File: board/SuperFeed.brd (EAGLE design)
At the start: 97.8 x 59.7 mm, 16 parts

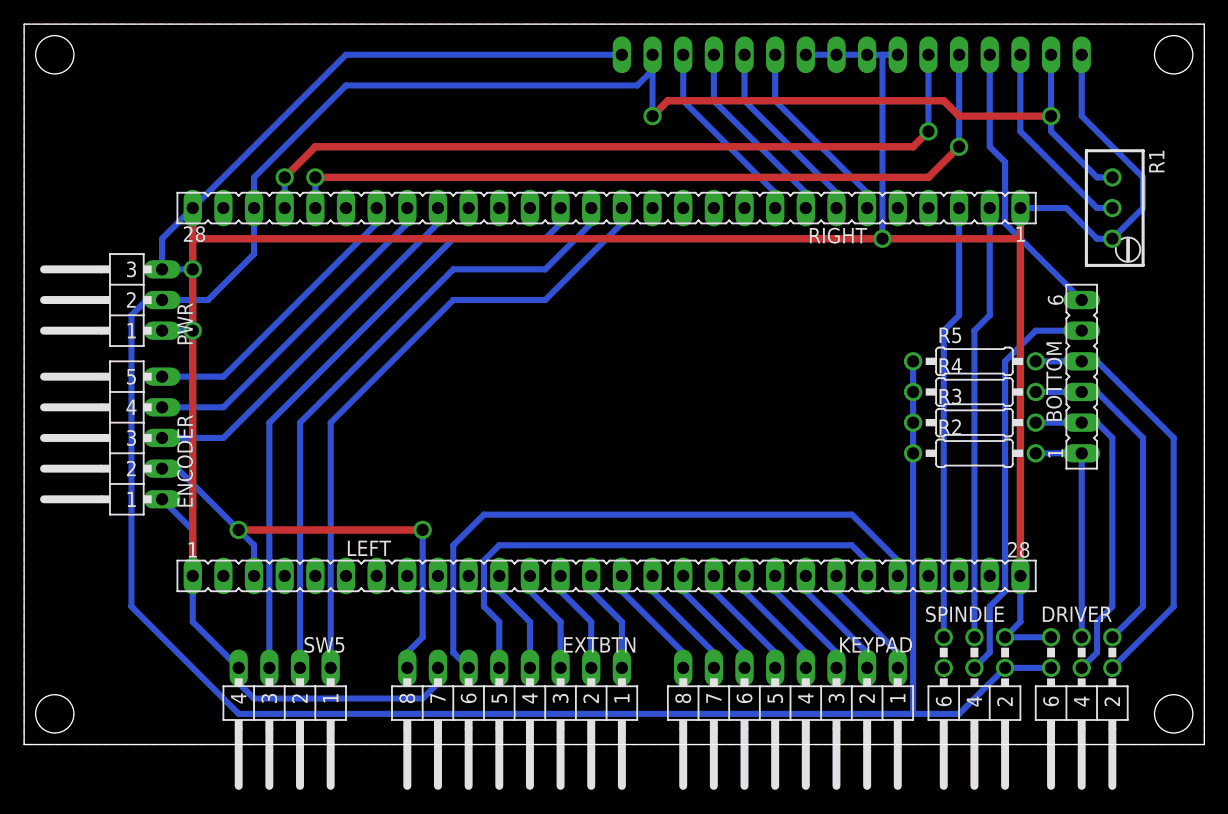
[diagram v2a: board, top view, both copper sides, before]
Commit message: Re-routing board to use GND plane on bottom side
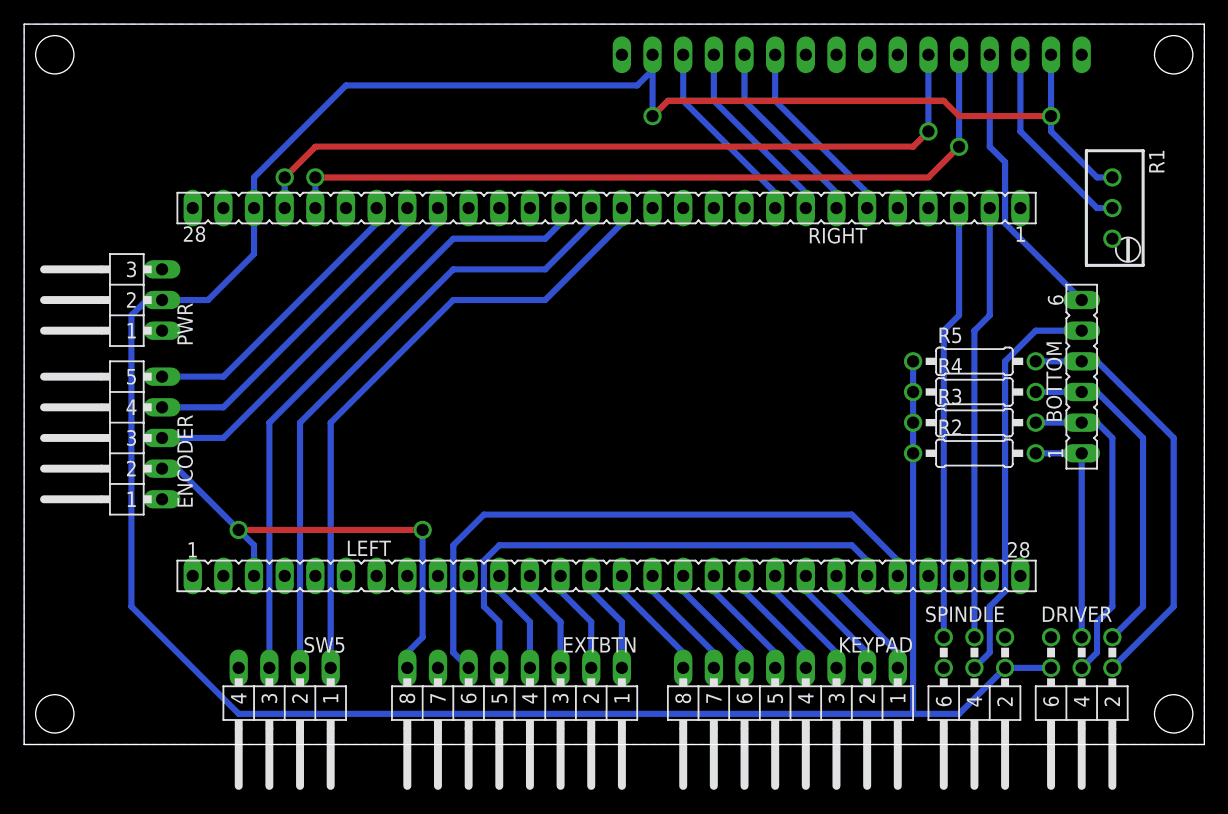
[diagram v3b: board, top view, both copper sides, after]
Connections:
- net GND: no longer PWR.1
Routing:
- net GND: track 278.9 -> 0.00 mm, vias 3 -> 0
- added copper zone on layer 16, net GND
- removed copper zone on layer 1, net GND
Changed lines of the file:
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@@
 <?xml version="1.0" encoding="utf-8"?>
 <!DOCTYPE eagle SYSTEM "eagle.dtd">
-<eagle version="6.2">
+<eagle version="6.6.0">
 <drawing>
 <settings>
@@
 <layer number="17" name="Pads" color="2" fill="1" visible="yes" active="yes"/>
 <layer number="18" name="Vias" color="2" fill="1" visible="yes" active="yes"/>
-<layer number="19" name="Unrouted" color="6" fill="1" visible="no" active="yes"/>
+<layer number="19" name="Unrouted" color="6" fill="1" visible="yes" active="yes"/>
 <layer number="20" name="Dimension" color="15" fill="1" visible="yes" active="yes"/>
 <layer number="21" name="tPlace" color="7" fill="1" visible="no" active="yes"/>
-<layer number="22" name="bPlace" color="7" fill="1" visible="no" active="yes"/>
-<layer number="23" name="tOrigins" color="15" fill="1" visible="no" active="yes"/>
-<layer number="24" name="bOrigins" color="15" fill="1" visible="no" active="yes"/>
+<layer number="22" name="bPlace" color="7" fill="1" visible="yes" active="yes"/>
+<layer number="23" name="tOrigins" color="15" fill="1" visible="yes" active="yes"/>
+<layer number="24" name="bOrigins" color="15" fill="1" visible="yes" active="yes"/>
 <layer number="25" name="tNames" color="7" fill="1" visible="no" active="yes"/>
 <layer number="26" name="bNames" color="7" fill="1" visible="no" active="yes"/>
@@
 <layer number="43" name="vRestrict" color="2" fill="10" visible="no" active="yes"/>
 <layer number="44" name="Drills" color="7" fill="1" visible="no" active="yes"/>
-<layer number="45" name="Holes" color="7" fill="1" visible="yes" active="yes"/>
+<layer number="45" name="Holes" color="7" fill="1" visible="no" active="yes"/>
 <layer number="46" name="Milling" color="3" fill="1" visible="no" active="yes"/>
 <layer number="47" name="Measures" color="7" fill="1" visible="no" active="yes"/>
@@
 </class>
 </classes>
-<designrules>
+<designrules name="default">
 <description language="de">&lt;b&gt;EAGLE Design Rules&lt;/b&gt;
 &lt;p&gt;
@@
 <contactref element="SPINDLE" pad="1"/>
 <contactref element="DRIVER" pad="5"/>
-<wire x1="85.09" y1="8.89" x2="81.28" y2="8.89" width="0.508" layer="16"/>
-<wire x1="82.55" y1="13.97" x2="82.55" y2="12.7" width="0.508" layer="16"/>
-<wire x1="64.77" y1="57.15" x2="67.31" y2="57.15" width="0.508" layer="16"/>
-<wire x1="67.31" y1="57.15" x2="69.85" y2="57.15" width="0.508" layer="16"/>
-<wire x1="69.85" y1="57.15" x2="71.12" y2="57.15" width="0.508" layer="16"/>
-<wire x1="13.97" y1="10.16" x2="13.97" y2="13.97" width="0.508" layer="16"/>
-<wire x1="13.97" y1="13.97" x2="13.97" y2="17.78" width="0.508" layer="16"/>
-<wire x1="13.97" y1="17.78" x2="11.43" y2="20.32" width="0.508" layer="16"/>
-<wire x1="49.53" y1="57.15" x2="26.67" y2="57.15" width="0.508" layer="16"/>
-<wire x1="82.55" y1="13.97" x2="82.55" y2="10.16" width="0.508" layer="16"/>
-<wire x1="82.55" y1="10.16" x2="81.28" y2="8.89" width="0.508" layer="16"/>
-<wire x1="82.55" y1="13.97" x2="82.55" y2="41.91" width="0.6096" layer="1"/>
-<wire x1="13.97" y1="13.97" x2="13.97" y2="34.29" width="0.6096" layer="1"/>
-<wire x1="13.97" y1="39.37" x2="13.97" y2="41.91" width="0.6096" layer="1"/>
-<wire x1="13.97" y1="41.91" x2="71.12" y2="41.91" width="0.6096" layer="1"/>
 <contactref element="R1" pad="3"/>
-<wire x1="82.55" y1="44.45" x2="86.36" y2="44.45" width="0.508" layer="16"/>
-<wire x1="86.36" y1="44.45" x2="88.9" y2="41.91" width="0.508" layer="16"/>
-<wire x1="88.9" y1="41.91" x2="90.17" y2="41.91" width="0.508" layer="16"/>
-<wire x1="87.63" y1="57.15" x2="87.63" y2="52.07" width="0.508" layer="16"/>
-<wire x1="87.63" y1="52.07" x2="92.71" y2="46.99" width="0.508" layer="16"/>
-<wire x1="92.71" y1="46.99" x2="92.71" y2="44.45" width="0.508" layer="16"/>
-<wire x1="92.71" y1="44.45" x2="90.17" y2="41.91" width="0.508" layer="16"/>
-<wire x1="17.78" y1="6.35" x2="13.97" y2="10.16" width="0.508" layer="16"/>
-<wire x1="72.39" y1="57.15" x2="71.12" y2="57.15" width="0.508" layer="16"/>
-<wire x1="71.12" y1="57.15" x2="71.12" y2="41.91" width="0.508" layer="16"/>
-<via x="71.12" y="41.91" extent="1-16" drill="1.016"/>
-<wire x1="82.55" y1="44.45" x2="82.55" y2="41.91" width="0.6096" layer="1"/>
-<wire x1="82.55" y1="41.91" x2="71.12" y2="41.91" width="0.6096" layer="1"/>
-<wire x1="13.97" y1="44.45" x2="13.97" y2="41.91" width="0.6096" layer="1"/>
-<contactref element="PWR" pad="1"/>
-<wire x1="11.43" y1="34.29" x2="13.97" y2="34.29" width="0.508" layer="16"/>
-<via x="13.97" y="34.29" extent="1-16" drill="1.016"/>
-<wire x1="11.43" y1="39.37" x2="13.97" y2="39.37" width="0.508" layer="16"/>
-<via x="13.97" y="39.37" extent="1-16" drill="1.016"/>
-<wire x1="13.97" y1="39.37" x2="13.97" y2="34.29" width="0.6096" layer="1"/>
-<wire x1="13.97" y1="44.45" x2="11.43" y2="41.91" width="0.508" layer="16"/>
-<wire x1="11.43" y1="39.37" x2="11.43" y2="41.91" width="0.508" layer="16"/>
-<wire x1="13.97" y1="44.45" x2="26.67" y2="57.15" width="0.508" layer="16"/>
-<polygon width="0.4064" layer="1" isolate="0.4064" rank="6">
+<contactref element="EXTBTN" pad="7"/>
+<polygon width="0.508" layer="16">
+<vertex x="0" y="59.69"/>
 <vertex x="97.79" y="59.69"/>
 <vertex x="97.79" y="0"/>
 <vertex x="0" y="0"/>
-<vertex x="0" y="59.69"/>
 </polygon>
-<contactref element="EXTBTN" pad="7"/>
-<wire x1="34.29" y1="6.35" x2="34.29" y2="5.08" width="0.508" layer="16"/>
-<wire x1="34.29" y1="5.08" x2="33.02" y2="3.81" width="0.508" layer="16"/>
-<wire x1="33.02" y1="3.81" x2="19.05" y2="3.81" width="0.508" layer="16"/>
-<wire x1="19.05" y1="3.81" x2="17.78" y2="5.08" width="0.508" layer="16"/>
-<wire x1="17.78" y1="5.08" x2="17.78" y2="6.35" width="0.508" layer="16"/>
+<wire x1="49.53" y1="57.15" x2="64.77" y2="57.15" width="0" layer="19" extent="1-1"/>
 </signal>
 <signal name="+5V">
@@
 <wire x1="85.09" y1="50.8" x2="85.09" y2="52.07" width="0.508" layer="16"/>
 <via x="85.09" y="52.07" extent="1-16" drill="1.016"/>
-<wire x1="85.09" y1="52.07" x2="77.47" y2="52.07" width="0.6096" layer="1"/>
-<wire x1="77.47" y1="52.07" x2="76.2" y2="53.34" width="0.6096" layer="1"/>
-<wire x1="76.2" y1="53.34" x2="53.34" y2="53.34" width="0.6096" layer="1"/>
-<wire x1="53.34" y1="53.34" x2="52.07" y2="52.07" width="0.6096" layer="1"/>
+<wire x1="85.09" y1="52.07" x2="77.47" y2="52.07" width="0.508" layer="1"/>
+<wire x1="77.47" y1="52.07" x2="76.2" y2="53.34" width="0.508" layer="1"/>
+<wire x1="76.2" y1="53.34" x2="53.34" y2="53.34" width="0.508" layer="1"/>
+<wire x1="53.34" y1="53.34" x2="52.07" y2="52.07" width="0.508" layer="1"/>
 <wire x1="11.43" y1="36.83" x2="15.24" y2="36.83" width="0.508" layer="16"/>
 <wire x1="15.24" y1="36.83" x2="19.05" y2="40.64" width="0.508" layer="16"/>
@@
 <wire x1="33.02" y1="8.89" x2="33.02" y2="17.78" width="0.508" layer="16"/>
 <via x="33.02" y="17.78" extent="1-16" drill="1.016"/>
-<wire x1="33.02" y1="17.78" x2="17.78" y2="17.78" width="0.6096" layer="1"/>
+<wire x1="33.02" y1="17.78" x2="17.78" y2="17.78" width="0.508" layer="1"/>
 <via x="17.78" y="17.78" extent="1-16" drill="1.016"/>
 <wire x1="17.78" y1="17.78" x2="19.05" y2="16.51" width="0.508" layer="16"/>
@@
 <wire x1="74.93" y1="57.15" x2="74.93" y2="50.8" width="0.508" layer="16"/>
 <via x="74.93" y="50.8" extent="1-16" drill="1.016"/>
-<wire x1="74.93" y1="50.8" x2="73.66" y2="49.53" width="0.6096" layer="1"/>
-<wire x1="73.66" y1="49.53" x2="24.13" y2="49.53" width="0.6096" layer="1"/>
-<wire x1="24.13" y1="49.53" x2="21.59" y2="46.99" width="0.6096" layer="1"/>
+<wire x1="74.93" y1="50.8" x2="73.66" y2="49.53" width="0.508" layer="1"/>
+<wire x1="73.66" y1="49.53" x2="24.13" y2="49.53" width="0.508" layer="1"/>
+<wire x1="24.13" y1="49.53" x2="21.59" y2="46.99" width="0.508" layer="1"/>
 <via x="21.59" y="46.99" extent="1-16" drill="1.016"/>
 <wire x1="21.59" y1="46.99" x2="21.59" y2="44.45" width="0.508" layer="16"/>
@@
 <wire x1="77.47" y1="57.15" x2="77.47" y2="49.53" width="0.508" layer="16"/>
 <via x="77.47" y="49.53" extent="1-16" drill="1.016"/>
-<wire x1="77.47" y1="49.53" x2="74.93" y2="46.99" width="0.6096" layer="1"/>
-<wire x1="74.93" y1="46.99" x2="24.13" y2="46.99" width="0.6096" layer="1"/>
+<wire x1="77.47" y1="49.53" x2="74.93" y2="46.99" width="0.508" layer="1"/>
+<wire x1="74.93" y1="46.99" x2="24.13" y2="46.99" width="0.508" layer="1"/>
 <via x="24.13" y="46.99" extent="1-16" drill="1.016"/>
 <wire x1="24.13" y1="46.99" x2="24.13" y2="44.45" width="0.508" layer="16"/>

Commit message: Custom design rules, moving pot a little bit
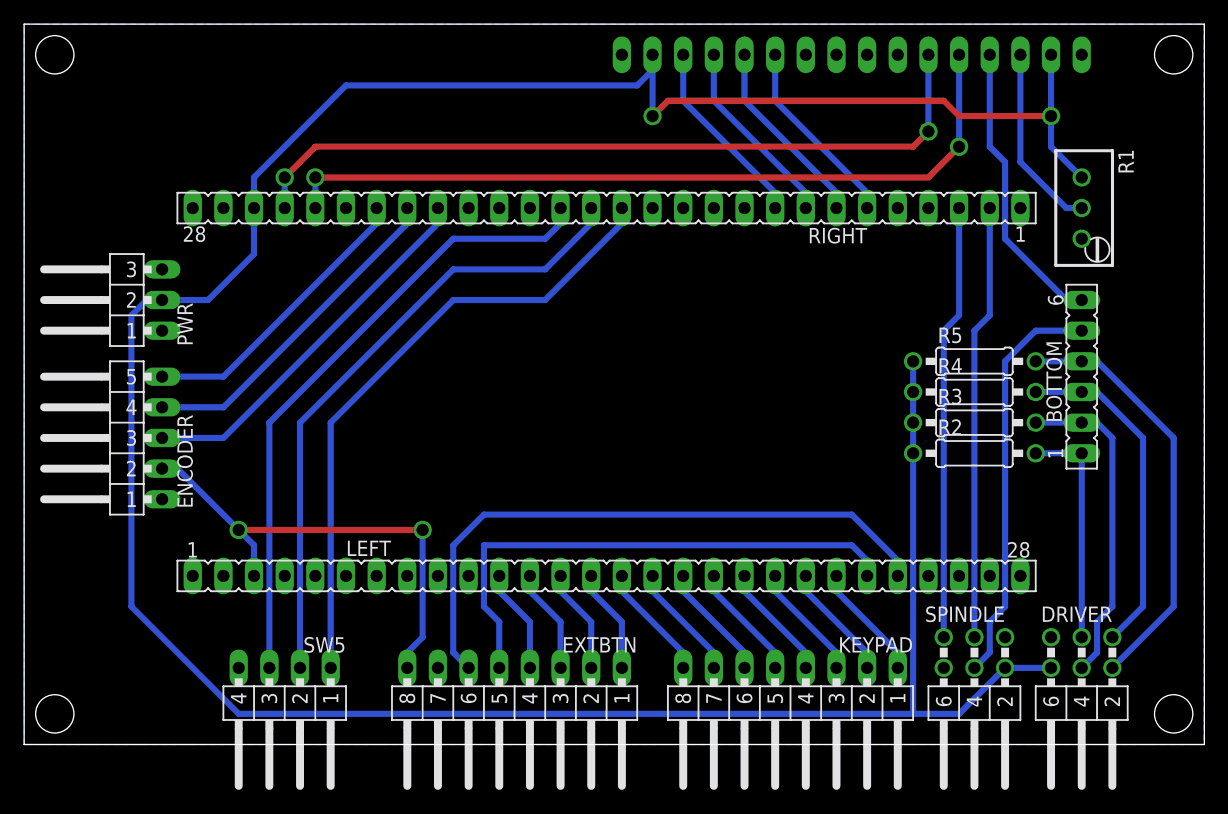
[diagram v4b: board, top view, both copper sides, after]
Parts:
- moved R1 2.54 mm to (87.6, 44.5)
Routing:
- net +5V: track 243.5 -> 241.8 mm
- net V0: track 16.6 -> 15.5 mm
- net PB15: track 23.5 -> 24.2 mm
- net PC4: track 43.5 -> 44.2 mm
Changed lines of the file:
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@@
 </class>
 </classes>
-<designrules name="default">
+<designrules name="SuperFeed">
 <description language="de">&lt;b&gt;EAGLE Design Rules&lt;/b&gt;
 &lt;p&gt;
@@
 <param name="mtCopper" value="0.035mm 0.035mm 0.035mm 0.035mm 0.035mm 0.035mm 0.035mm 0.035mm 0.035mm 0.035mm 0.035mm 0.035mm 0.035mm 0.035mm 0.035mm 0.035mm"/>
 <param name="mtIsolate" value="1.5mm 0.15mm 0.2mm 0.15mm 0.2mm 0.15mm 0.2mm 0.15mm 0.2mm 0.15mm 0.2mm 0.15mm 0.2mm 0.15mm 0.2mm"/>
-<param name="mdWireWire" value="8mil"/>
-<param name="mdWirePad" value="8mil"/>
-<param name="mdWireVia" value="8mil"/>
-<param name="mdPadPad" value="8mil"/>
-<param name="mdPadVia" value="8mil"/>
-<param name="mdViaVia" value="8mil"/>
-<param name="mdSmdPad" value="8mil"/>
-<param name="mdSmdVia" value="8mil"/>
-<param name="mdSmdSmd" value="8mil"/>
+<param name="mdWireWire" value="10mil"/>
+<param name="mdWirePad" value="10mil"/>
+<param name="mdWireVia" value="10mil"/>
+<param name="mdPadPad" value="10mil"/>
+<param name="mdPadVia" value="10mil"/>
+<param name="mdViaVia" value="10mil"/>
+<param name="mdSmdPad" value="10mil"/>
+<param name="mdSmdVia" value="10mil"/>
+<param name="mdSmdSmd" value="10mil"/>
 <param name="mdViaViaSameLayer" value="8mil"/>
 <param name="mnLayersViaInSmd" value="2"/>
 <param name="mdCopperDimension" value="40mil"/>
-<param name="mdDrill" value="8mil"/>
+<param name="mdDrill" value="10mil"/>
 <param name="mdSmdStop" value="0mil"/>
-<param name="msWidth" value="10mil"/>
+<param name="msWidth" value="16mil"/>
 <param name="msDrill" value="24mil"/>
 <param name="msMicroVia" value="9.99mm"/>
@@
 <param name="srMaxRoundness" value="0mil"/>
 <param name="slThermalIsolate" value="10mil"/>
-<param name="slThermalsForVias" value="0"/>
+<param name="slThermalsForVias" value="1"/>
 <param name="dpMaxLengthDifference" value="10mm"/>
 <param name="dpGapFactor" value="2.5"/>
@@
 <element name="PWR" library="SuperFeed" package="MA03-1W" value="" x="11.43" y="36.83" rot="R90"/>
 <element name="SPINDLE" library="SuperFeed" package="MA03-2W" value="" x="78.74" y="7.62" rot="R180"/>
-<element name="R1" library="SuperFeed" package="RTRIMT93YA" value="" x="90.17" y="44.45" rot="R180"/>
+<element name="R1" library="SuperFeed" package="RTRIMT93YA" value="" x="87.63" y="44.45" rot="R180"/>
 <element name="R2" library="SuperFeed" package="0207/10" value="10k" x="78.74" y="24.13"/>
 <element name="R3" library="SuperFeed" package="0207/10" value="10k" x="78.74" y="26.67"/>
@@
 <vertex x="0" y="0"/>
 </polygon>
-<wire x1="49.53" y1="57.15" x2="64.77" y2="57.15" width="0" layer="19" extent="1-1"/>
+<wire x1="64.77" y1="57.15" x2="49.53" y2="57.15" width="0" layer="19" extent="1-1"/>
 </signal>
 <signal name="+5V">
@@
 <contactref element="R1" pad="1"/>
 <contactref element="LCD" pad="2"/>
-<wire x1="90.17" y1="46.99" x2="88.9" y2="46.99" width="0.508" layer="16"/>
-<wire x1="88.9" y1="46.99" x2="85.09" y2="50.8" width="0.508" layer="16"/>
 <wire x1="85.09" y1="52.07" x2="85.09" y2="57.15" width="0.508" layer="16"/>
 <contactref element="R5" pad="1"/>
@@
 <wire x1="73.66" y1="29.21" x2="73.66" y2="26.67" width="0.508" layer="16"/>
 <wire x1="73.66" y1="24.13" x2="73.66" y2="2.54" width="0.508" layer="16"/>
-<wire x1="85.09" y1="50.8" x2="85.09" y2="52.07" width="0.508" layer="16"/>
 <via x="85.09" y="52.07" extent="1-16" drill="1.016"/>
 <wire x1="85.09" y1="52.07" x2="77.47" y2="52.07" width="0.508" layer="1"/>
@@
 <wire x1="17.78" y1="2.54" x2="8.89" y2="11.43" width="0.508" layer="16"/>
 <wire x1="8.89" y1="11.43" x2="8.89" y2="35.56" width="0.508" layer="16"/>
+<wire x1="85.09" y1="52.07" x2="85.09" y2="49.53" width="0.508" layer="16"/>
+<wire x1="85.09" y1="49.53" x2="87.63" y2="46.99" width="0.508" layer="16"/>
 </signal>
 <signal name="NC">
@@
 <wire x1="39.37" y1="6.35" x2="39.37" y2="10.16" width="0.508" layer="16"/>
 <wire x1="39.37" y1="10.16" x2="38.1" y2="11.43" width="0.508" layer="16"/>
-<wire x1="38.1" y1="11.43" x2="38.1" y2="15.24" width="0.508" layer="16"/>
-<wire x1="38.1" y1="15.24" x2="39.37" y2="16.51" width="0.508" layer="16"/>
-<wire x1="39.37" y1="16.51" x2="68.58" y2="16.51" width="0.508" layer="16"/>
+<wire x1="38.1" y1="11.43" x2="38.1" y2="16.51" width="0.508" layer="16"/>
+<wire x1="38.1" y1="16.51" x2="68.58" y2="16.51" width="0.508" layer="16"/>
 <wire x1="68.58" y1="16.51" x2="69.85" y2="15.24" width="0.508" layer="16"/>
 <wire x1="69.85" y1="15.24" x2="69.85" y2="13.97" width="0.508" layer="16"/>
@@
 <contactref element="SPINDLE" pad="4"/>
 <wire x1="78.74" y1="6.35" x2="80.01" y2="7.62" width="0.508" layer="16"/>
-<wire x1="80.01" y1="7.62" x2="80.01" y2="11.43" width="0.508" layer="16"/>
-<wire x1="80.01" y1="11.43" x2="81.28" y2="12.7" width="0.508" layer="16"/>
-<wire x1="81.28" y1="12.7" x2="81.28" y2="31.75" width="0.508" layer="16"/>
+<wire x1="80.01" y1="7.62" x2="80.01" y2="10.16" width="0.508" layer="16"/>
+<wire x1="80.01" y1="10.16" x2="81.28" y2="11.43" width="0.508" layer="16"/>
+<wire x1="81.28" y1="11.43" x2="81.28" y2="31.75" width="0.508" layer="16"/>
 <wire x1="87.63" y1="34.29" x2="83.82" y2="34.29" width="0.508" layer="16"/>
 <wire x1="83.82" y1="34.29" x2="81.28" y2="31.75" width="0.508" layer="16"/>
@@
 <wire x1="80.01" y1="57.15" x2="80.01" y2="49.53" width="0.508" layer="16"/>
 <wire x1="80.01" y1="49.53" x2="81.28" y2="48.26" width="0.508" layer="16"/>
-<wire x1="81.28" y1="48.26" x2="81.28" y2="43.18" width="0.508" layer="16"/>
-<wire x1="81.28" y1="43.18" x2="87.63" y2="36.83" width="0.508" layer="16"/>
+<wire x1="81.28" y1="48.26" x2="81.28" y2="41.91" width="0.508" layer="16"/>
+<wire x1="81.28" y1="41.91" x2="86.36" y2="36.83" width="0.508" layer="16"/>
+<wire x1="86.36" y1="36.83" x2="87.63" y2="36.83" width="0.508" layer="16"/>
 </signal>
 <signal name="NC2">
@@
 <contactref element="LCD" pad="3"/>
 <contactref element="R1" pad="2"/>
-<wire x1="90.17" y1="44.45" x2="88.9" y2="44.45" width="0.508" layer="16"/>
-<wire x1="88.9" y1="44.45" x2="82.55" y2="50.8" width="0.508" layer="16"/>
-<wire x1="82.55" y1="50.8" x2="82.55" y2="57.15" width="0.508" layer="16"/>
+<wire x1="82.55" y1="48.26" x2="82.55" y2="57.15" width="0.508" layer="16"/>
+<wire x1="82.55" y1="48.26" x2="86.36" y2="44.45" width="0.508" layer="16"/>
+<wire x1="86.36" y1="44.45" x2="87.63" y2="44.45" width="0.508" layer="16"/>
 </signal>
 </signals>

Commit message: Minor improvements to the board
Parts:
- moved KEYPAD 2.84 mm to (62.2, 3.81)
- moved EXTBTN 2.54 mm to (40.6, 3.81)
- moved SW5 2.54 mm to (21.6, 3.81)
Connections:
- net GND: now also PWR.1
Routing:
- net +5V: track 241.8 -> 185.0 mm
- net PC12: track 52.6 -> 55.1 mm
- net +3V3: track 40.0 -> 42.5 mm
- net PC5: track 51.4 -> 54.0 mm
- net PC3: track 8.67 -> 11.2 mm
- net PC2: track 8.67 -> 11.2 mm
- net PC11: track 52.6 -> 55.1 mm
- net PC10: track 52.6 -> 55.1 mm
- net PC1: track 8.67 -> 11.2 mm
- net PC0: track 8.67 -> 11.2 mm
- net PC4: track 44.2 -> 46.8 mm
- net PA7: track 9.72 -> 11.7 mm
- net PA6: track 9.72 -> 11.7 mm
- net PA5: track 9.72 -> 11.7 mm
- net PA4: track 9.72 -> 11.7 mm
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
